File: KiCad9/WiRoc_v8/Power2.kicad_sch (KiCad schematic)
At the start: 21 parts, among them U15 RT8059, U16 RT8059, U17 RT8059

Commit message: etc
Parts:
- C65: LCSC Part # (none) -> C15525; Manufacturer (none) -> Samsung Electro-Mechanics; ManufacturerPartNumber (none) -> CL05A106MQ5NUNC
- R42, R46: LCSC Part # (none) -> C25804; Manufacturer (none) -> Uniroyal Elec; ManufacturerPartNumber (none) -> 0603WAF1002T5E
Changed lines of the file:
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@@
+			)
+		)
+		(property "LCSC Part #" "C15525"
+			(at 147.32 76.2 0)
+			(effects
+				(font
+					(size 1.27 1.27)
+				)
+				(hide yes)
+			)
+		)
+		(property "Manufacturer" "Samsung Electro-Mechanics"
+			(at 147.32 76.2 0)
+			(effects
+				(font
+					(size 1.27 1.27)
+				)
+				(hide yes)
+			)
+		)
+		(property "ManufacturerPartNumber" "CL05A106MQ5NUNC"
+			(at 147.32 76.2 0)
+			(effects
+				(font
+					(size 1.27 1.27)
+				)
+				(hide yes)
 			)
 		)
@@
 			)
 		)
+		(property "LCSC Part #" "C25804"
+			(at 81.28 67.31 0)
+			(effects
+				(font
+					(size 1.27 1.27)
+				)
+				(hide yes)
+			)
+		)
+		(property "Manufacturer" "Uniroyal Elec"
+			(at 81.28 67.31 0)
+			(effects
+				(font
+					(size 1.27 1.27)
+				)
+				(hide yes)
+			)
+		)
+		(property "ManufacturerPartNumber" "0603WAF1002T5E"
+			(at 81.28 67.31 0)
+			(effects
+				(font
+					(size 1.27 1.27)
+				)
+				(hide yes)
+			)
+		)
 		(pin "2"
 		)
@@
 			(at 81.28 113.03 0)
 			(effects
+				(font
+					(size 1.27 1.27)
+				)
+				(hide yes)
+			)
+		)
+		(property "LCSC Part #" "C25804"
+			(at 81.28 113.03 0)
+			(effects
+				(font
+					(size 1.27 1.27)
+				)
+				(hide yes)
+			)
+		)
+		(property "Manufacturer" "Uniroyal Elec"
+			(at 81.28 113.03 0)
+			(effects
+				(font
+					(size 1.27 1.27)
+				)
+				(hide yes)
+			)
+		)
+		(property "ManufacturerPartNumber" "0603WAF1002T5E"
+			(at 81.28 113.03 0)
+			(effects

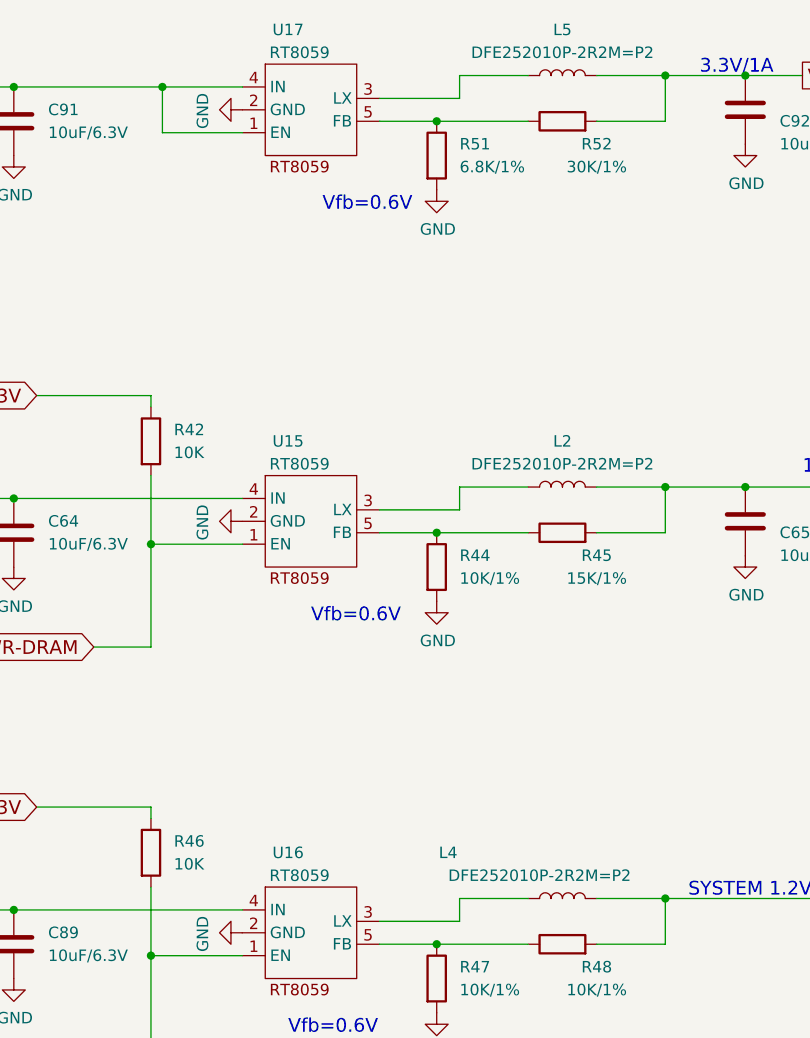
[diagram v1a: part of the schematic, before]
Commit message: add bom
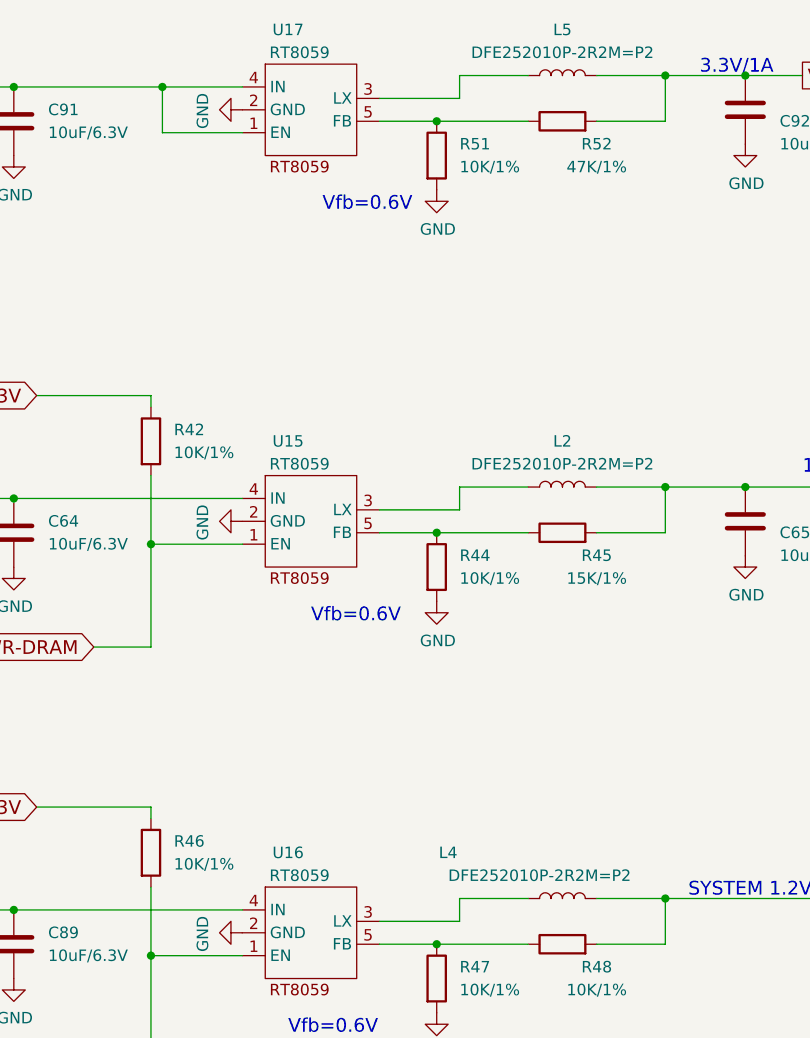
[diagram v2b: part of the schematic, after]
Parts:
- C64, C89, C90, C91, C92: IncludeInBOM (none) -> TRUE; JLCBasicExtended (none) -> Basic; LCSC Part # (none) -> C15525; Manufacturer (none) -> Samsung Electro-Mechanics; ManufacturerPartNumber (none) -> CL05A106MQ5NUNC; Package (none) -> 0402
- C65: IncludeInBOM (none) -> TRUE; JLCBasicExtended (none) -> Basic; Package (none) -> 0402
- L2, L4, L5: IncludeInBOM (none) -> TRUE; JLCBasicExtended (none) -> Extended; LCSC Part # (none) -> C882952; Manufacturer (none) -> Murata Electronics; ManufacturerPartNumber (none) -> DFE252010P-2R2M=P2; Package (none) -> 1008
- R42, R46: value 10K -> 10K/1%; IncludeInBOM (none) -> TRUE; JLCBasicExtended (none) -> Basic; LCSC Part # C25804 -> C25744; ManufacturerPartNumber 0603WAF1002T5E -> 0402WGF1002TCE; Package (none) -> 0402
- R44, R47, R48: IncludeInBOM (none) -> TRUE; JLCBasicExtended (none) -> Basic; LCSC Part # (none) -> C25744; Manufacturer (none) -> Uniroyal Elec; ManufacturerPartNumber (none) -> 0402WGF1002TCE; Package (none) -> 0402
- R45: IncludeInBOM (none) -> TRUE; JLCBasicExtended (none) -> Basic; LCSC Part # (none) -> C25756; Manufacturer (none) -> Uniroyal Elec; ManufacturerPartNumber (none) -> 0402WGF1502TCE; Package (none) -> 0402
- R49: IncludeInBOM (none) -> TRUE; JLCBasicExtended (none) -> Extended; LCSC Part # (none) -> C25157; Manufacturer (none) -> Uniroyal Elec; ManufacturerPartNumber (none) -> 0402WGJ020JTCE; Package (none) -> 0402
- R51: value 6.8K/1% -> 10K/1%; IncludeInBOM (none) -> TRUE; JLCBasicExtended (none) -> Basic; LCSC Part # (none) -> C25744; Manufacturer (none) -> Uniroyal Elec; ManufacturerPartNumber (none) -> 0402WGF1002TCE; Package (none) -> 0402
- R52: value 30K/1% -> 47K/1%; IncludeInBOM (none) -> TRUE; JLCBasicExtended (none) -> Basic; LCSC Part # (none) -> C25792; Manufacturer (none) -> Uniroyal Elec; ManufacturerPartNumber (none) -> 0402WGF4702TCE; Package (none) -> 0402
- U15, U16, U17: IncludeInBOM (none) -> TRUE; JLCBasicExtended (none) -> Extended; LCSC Part # (none) -> C20542; Manufacturer (none) -> Richtek Tech; ManufacturerPartNumber (none) -> RT8059GJ5; Package (none) -> TSOT-23-5

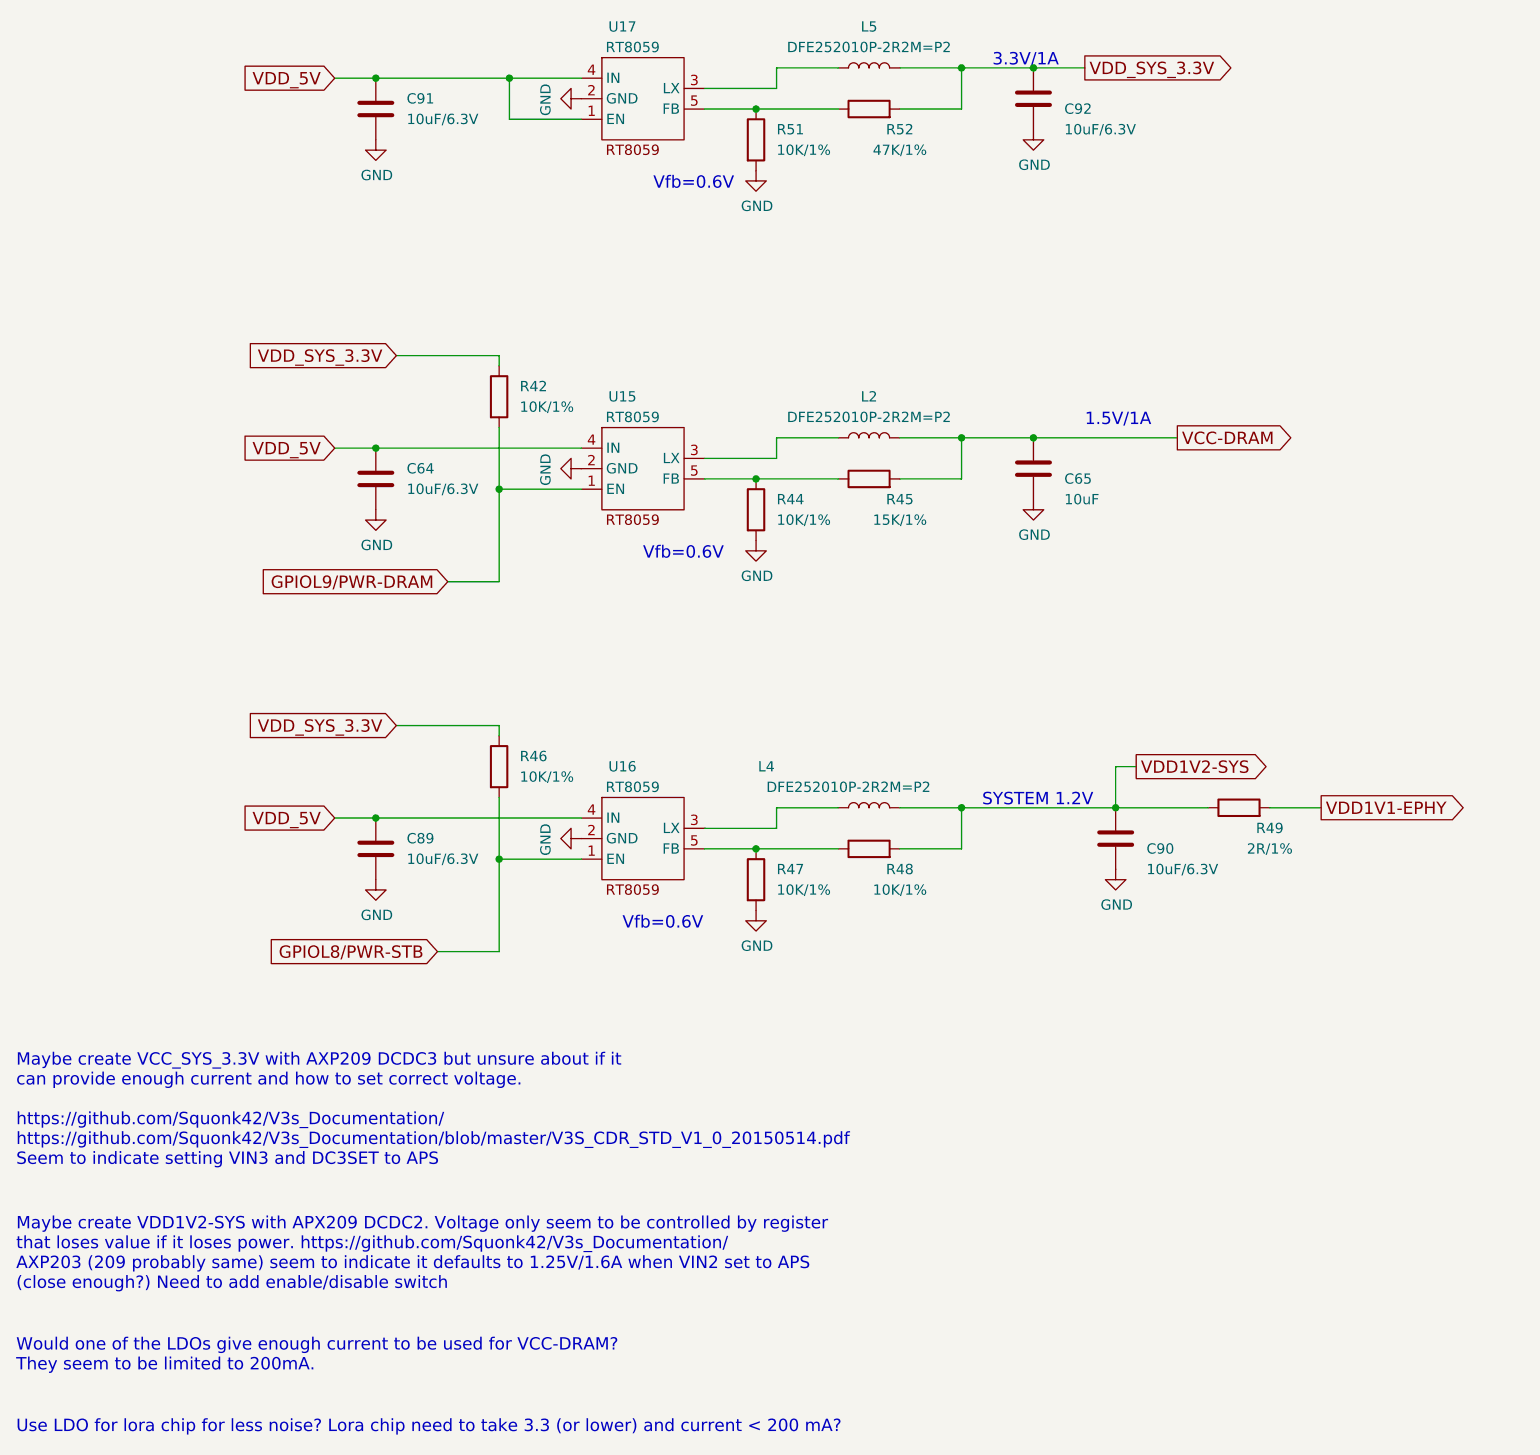
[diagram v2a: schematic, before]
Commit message: add esp32hosted-c5 board
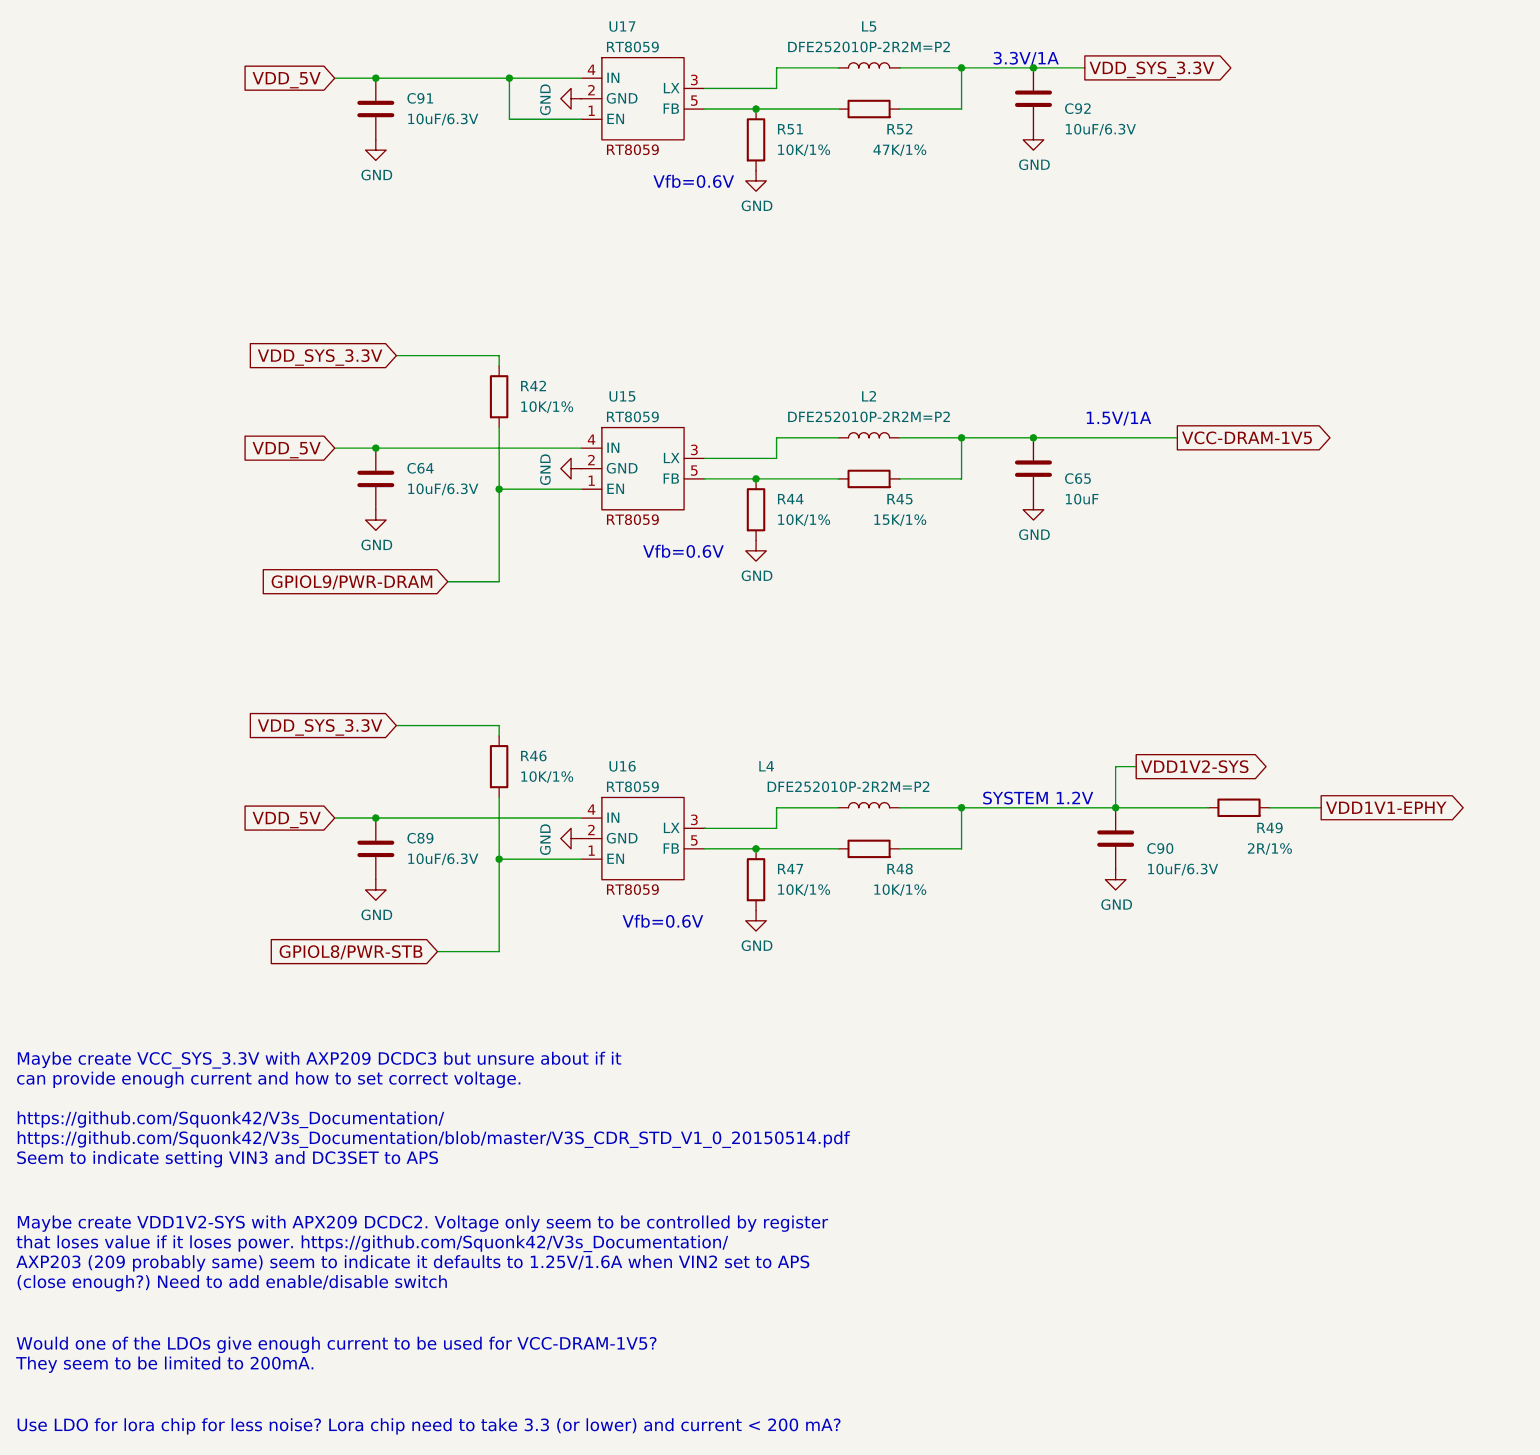
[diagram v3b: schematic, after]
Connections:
- net VCC-DRAM renamed VCC-DRAM-1V5
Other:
- note added: "Would one of the LDOs give enough current to be used for VCC-DRAM-1V5? They seem to be limited to 200mA."
- note removed: "Would one of the LDOs give enough current to be used for VCC-DRAM? They seem to be limited to 200mA."
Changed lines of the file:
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@@
 		)
 	)
-	(text "Would one of the LDOs give enough current to be used for VCC-DRAM?\nThey seem to be limited to 200mA.\n"
+	(text "Would one of the LDOs give enough current to be used for VCC-DRAM-1V5?\nThey seem to be limited to 200mA.\n"
 		(exclude_from_sim no)
 		(at 21.59 187.96 0)
@@
 		)
 	)
-	(global_label "VCC-DRAM"
+	(global_label "VCC-DRAM-1V5"
 		(shape output)
 		(at 165.1 72.39 0)
@@
 		)
 		(property "Intersheetrefs" "${INTERSHEET_REFS}"
-			(at 180.234 72.39 0)
+			(at 186.33 72.39 0)
 			(effects
 				(font
